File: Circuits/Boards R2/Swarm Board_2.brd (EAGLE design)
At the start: 54.9 x 63.6 mm, 94 parts, among them CON1 ISP(2X3), CON2 MAIN_CONNECTOR, CON3 FTDI_3PIN, CON4 POWERJUMPER, T1 NPN2N2222, T10 TEFT4300, T11 NPN2N2222, T13 NPN2N2222, T14 NPN2N2222, T15 NPN2N2222, T16 NPN2N2222, T17 NPN2N2222, T18 NPN2N2222, T2 NPN2N2222, T3 NPN2N2222, T4 TEFT4300, T5 TEFT4300, T6 TEFT4300, T7 TEFT4300, T8 TEFT4300, T9 TEFT4300, U1 ATMEGA324P, U2 MCP73833

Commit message: updated R2 board
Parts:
- CON4: value POWERJUMPER -> HEADER_3X1; device Mechanical:PINHEADER(1X2) -> Mechanical:3PINHEADER_.100"
- moved CON4 1.27 mm to (21.6, 37.8)
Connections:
- net +VBAT: now also CON4.2; no longer CON4.1
- net N$29: now also CON4.1; no longer CON4.2
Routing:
- net N$29: track 11.7 -> 17.9 mm
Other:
- board text added: "+3V"
- board text added: "B+"
- board text added: "B-"
- board text added: "MA+"
- board text added: "MA-"
- board text added: "MB+"
- board text added: "MB-"
- board text added: "PA1"
- board text added: "PA2"
- board text added: "PA3"
- board text added: "PA4T"
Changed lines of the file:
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@@
 <?xml version="1.0" encoding="utf-8"?>
 <!DOCTYPE eagle SYSTEM "eagle.dtd">
-<eagle version="6.2">
+<eagle version="6.3">
 <drawing>
 <settings>
@@
 <wire x1="4.318" y1="47.625" x2="59.182" y2="47.625" width="0.2032" layer="20" curve="-120"/>
 <wire x1="4.318" y1="15.748" x2="59.182" y2="15.748" width="0.2032" layer="20" curve="120"/>
+<text x="27.051" y="48.387" size="0.8128" layer="22" rot="MR270">B+</text>
+<text x="27.178" y="42.164" size="0.8128" layer="22" rot="MR270">B-</text>
+<text x="30.353" y="46.863" size="0.8128" layer="22" rot="MR90">GND</text>
+<text x="28.321" y="46.863" size="0.8128" layer="22" rot="MR90">+3V</text>
+<text x="37.338" y="42.164" size="0.8128" layer="22" rot="MR270">MB-</text>
+<text x="35.179" y="42.164" size="0.8128" layer="22" rot="MR270">MB+</text>
+<text x="37.211" y="49.149" size="0.8128" layer="22" rot="MR270">MA-</text>
+<text x="35.179" y="49.149" size="0.8128" layer="22" rot="MR270">MA+</text>
+<text x="33.02" y="49.911" size="0.8128" layer="22" rot="MR270">PA4T</text>
+<text x="29.21" y="42.164" size="0.8128" layer="22" rot="MR270">PA3</text>
+<text x="31.242" y="42.164" size="0.8128" layer="22" rot="MR270">PA2</text>
+<text x="33.274" y="42.164" size="0.8128" layer="22" rot="MR270">PA1</text>
 </plain>
 <attributes>
@@
 </class>
 </classes>
-<designrules>
+<designrules name="default">
 <description language="en">&lt;b&gt;EAGLE Design Rules&lt;/b&gt;
 &lt;p&gt;
@@
 </element>
 <element name="B1" library="Passive" package="PIEZOBUZZER" value="PIEZOBUZZERPTH" x="41.402" y="10.033"/>
-<element name="CON4" library="Mechanical" package="PINHEADER(1X2)" value="POWERJUMPER" x="21.59" y="39.116" rot="R90"/>
+<element name="CON4" library="Mechanical" package="3PINHEADER_.100&quot;" value="HEADER_3X1" x="21.59" y="37.846" rot="R90"/>
 </elements>
 <signals>
@@
 <wire x1="10.541" y1="17.950146875" x2="10.16" y2="18.542" width="0.254" layer="1"/>
 <wire x1="10.541" y1="17.950146875" x2="5.7785" y2="15.6845" width="0.4064" layer="16"/>
-<wire x1="11.944" y1="44.435478125" x2="13.6906" y2="43.64485" width="0.254" layer="1"/>
-<wire x1="11.944" y1="44.435478125" x2="9.271" y2="43.350146875" width="0.254" layer="1"/>
+<wire x1="11.944" y1="44.435478125" x2="13.6906" y2="43.64485" width="0.4064" layer="1"/>
+<wire x1="11.944" y1="44.435478125" x2="9.271" y2="43.350146875" width="0.4064" layer="1"/>
 <wire x1="5.461" y1="39.624" x2="9.187146875" y2="43.350146875" width="0.4064" layer="16"/>
 <wire x1="9.187146875" y1="43.350146875" x2="9.271" y2="43.350146875" width="0.3048" layer="16"/>
@@
 <wire x1="38.608" y1="24.765" x2="38.608" y2="25.997" width="0.3048" layer="1"/>
 <wire x1="38.608" y1="30.734" x2="38.608" y2="25.997" width="0.3048" layer="1"/>
-<wire x1="35.814" y1="32.547" x2="35.814" y2="30.734" width="0.3048" layer="1"/>
 <wire x1="27.559" y1="27.547" x2="27.297" y2="27.678" width="0.254" layer="1"/>
 <wire x1="27.297" y1="27.678" x2="25.908" y2="26.289" width="0.3048" layer="1"/>
@@
 <wire x1="45.593" y1="35.814" x2="46.482" y2="35.814" width="0.3048" layer="1"/>
 <wire x1="46.482" y1="35.814" x2="49.784" y2="39.116" width="0.3048" layer="1"/>
-<wire x1="35.814" y1="30.734" x2="38.608" y2="30.734" width="0.3048" layer="1"/>
 <wire x1="46.431" y1="43.266" x2="48.047" y2="43.266" width="0.3048" layer="1"/>
 <wire x1="48.047" y1="43.266" x2="48.895" y2="42.418" width="0.3048" layer="1"/>
@@
 <wire x1="49.784" y1="40.894" x2="48.907" y2="41.771" width="0.3048" layer="1"/>
 <wire x1="48.907" y1="41.771" x2="48.895" y2="41.771" width="0.3048" layer="1"/>
+<wire x1="35.814" y1="32.547" x2="35.814" y2="31.369" width="0.254" layer="1"/>
+<wire x1="35.814" y1="31.369" x2="36.449" y2="30.734" width="0.254" layer="1"/>
+<wire x1="36.449" y1="30.734" x2="38.608" y2="30.734" width="0.254" layer="1"/>
 </signal>
 <signal name="GND">
@@
 <wire x1="14.605" y1="30.341" x2="14.605" y2="31" width="0.254" layer="1"/>
 <wire x1="14.605" y1="31" x2="13.728" y2="31.877" width="0.254" layer="1"/>
-<contactref element="CON4" pad="1"/>
-<wire x1="21.59" y1="37.846" x2="20.955" y2="37.846" width="0.4064" layer="16"/>
 <wire x1="20.955" y1="37.846" x2="17.907" y2="40.894" width="0.4064" layer="16"/>
 <wire x1="17.907" y1="40.894" x2="16.637" y2="40.894" width="0.4064" layer="16"/>
+<contactref element="CON4" pad="2"/>
+<wire x1="20.955" y1="37.846" x2="21.59" y2="37.846" width="0.4064" layer="16"/>
 </signal>
 <signal name="+VCHG">
@@
 <signal name="N$29">
 <contactref element="CON2" pad="7"/>
-<contactref element="CON4" pad="2"/>
 <wire x1="26.75" y1="45.45" x2="20.939" y2="45.45" width="0.4064" layer="1"/>
 <wire x1="20.939" y1="45.45" x2="20.32" y2="44.831" width="0.4064" layer="1"/>
 <wire x1="20.32" y1="44.831" x2="20.32" y2="43.688" width="0.4064" layer="1"/>
-<wire x1="20.32" y1="43.688" x2="21.59" y2="42.418" width="0.4064" layer="1"/>
-<wire x1="21.59" y1="42.418" x2="21.59" y2="40.386" width="0.4064" layer="1"/>
+<contactref element="CON4" pad="1"/>
+<wire x1="20.32" y1="43.688" x2="22.987" y2="41.021" width="0.4064" layer="1"/>
+<wire x1="22.987" y1="41.021" x2="22.987" y2="36.703" width="0.4064" layer="1"/>
+<wire x1="22.987" y1="36.703" x2="21.59" y2="35.306" width="0.4064" layer="1"/>
 </signal>
 </signals>

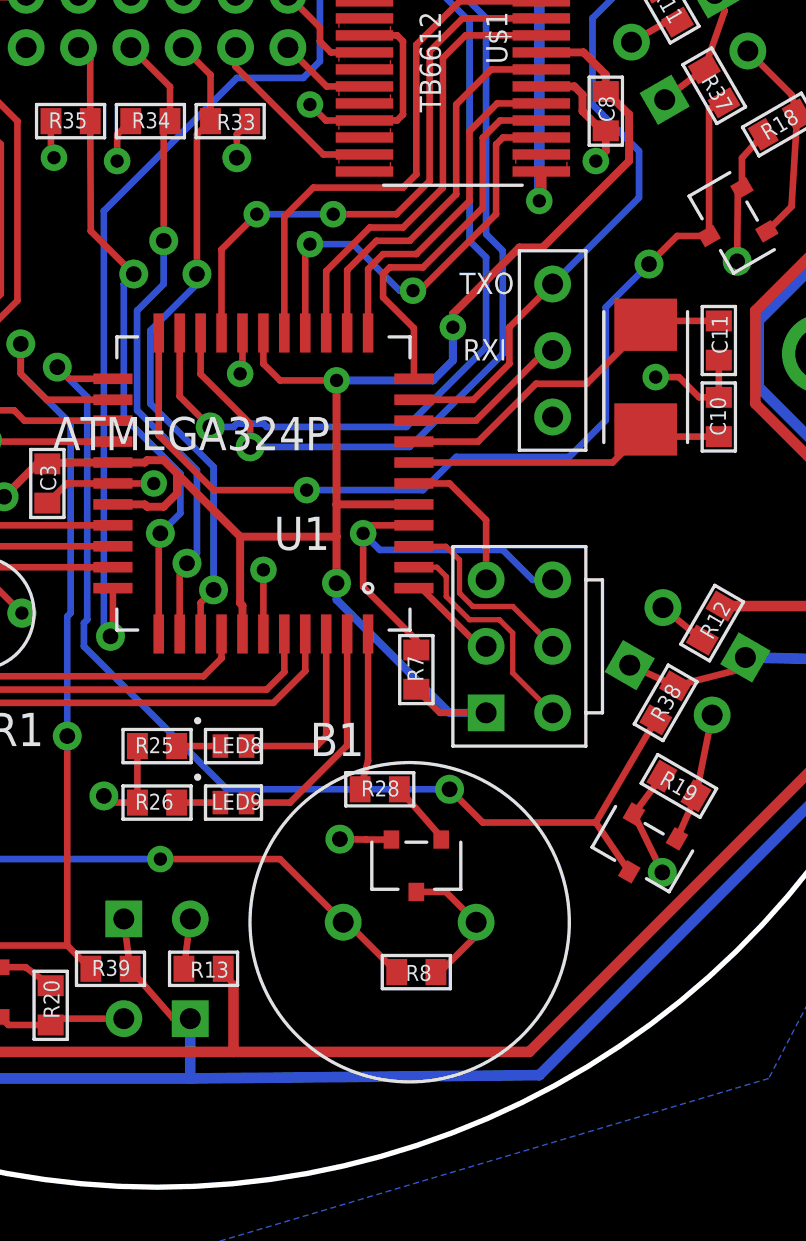
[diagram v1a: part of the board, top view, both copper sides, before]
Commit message: changed spacing on ISP header
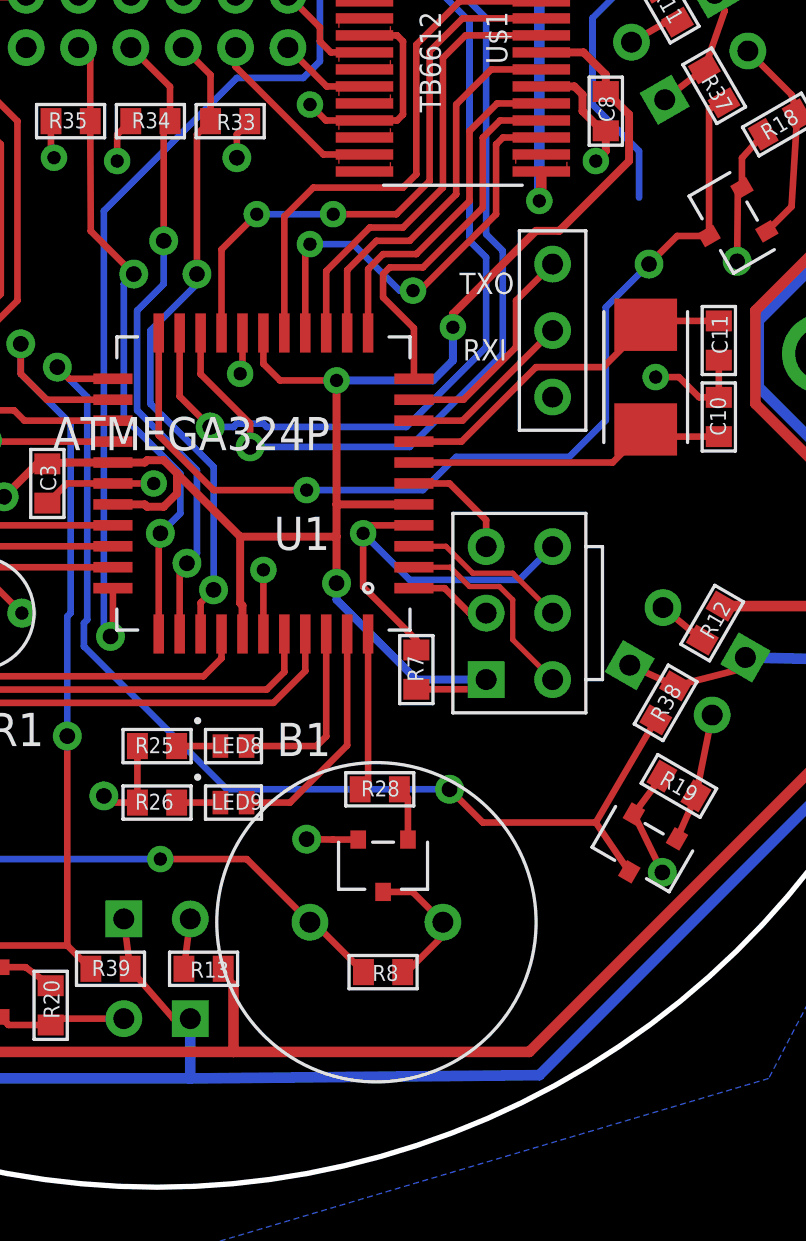
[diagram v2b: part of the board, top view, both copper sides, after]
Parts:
- moved B1 1.27 mm to (40.1, 10.0)
- moved CON1 1.27 mm to (45.6, 21.8)
- moved R8 1.27 mm to (40.4, 8.13)
- moved T1 1.27 mm to (40.4, 12.2)
- moved CON3 0.76 mm to (46.9, 32.6)
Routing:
- net DATAANTENNA: track 32.2 -> 28.1 mm
- net +3V: track 378.4 -> 376.4 mm
- net N$5: track 7.63 -> 6.36 mm
- net GND: track 116.0 -> 114.7 mm
- net N$3: track 8.94 -> 7.97 mm
- net N$26: track 2.76 -> 2.06 mm
- net N$6: track 15.3 -> 15.9 mm

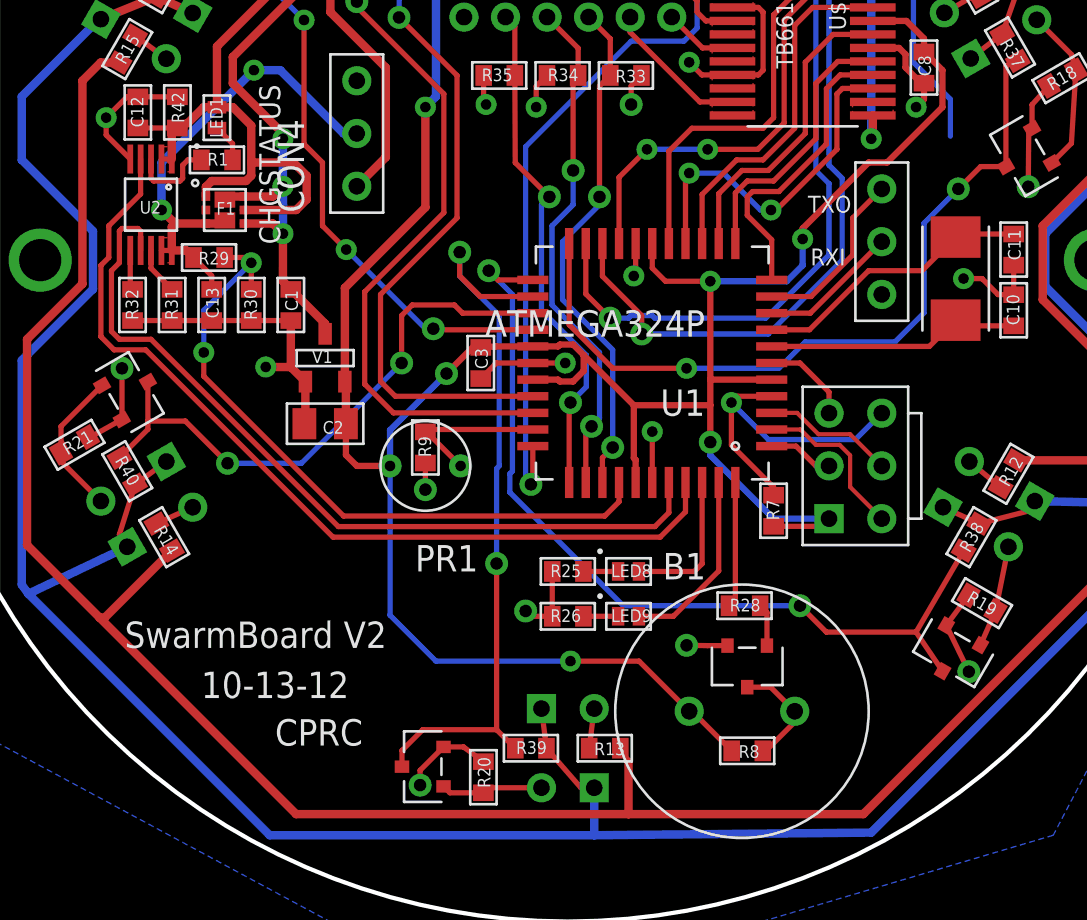
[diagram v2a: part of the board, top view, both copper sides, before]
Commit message: 
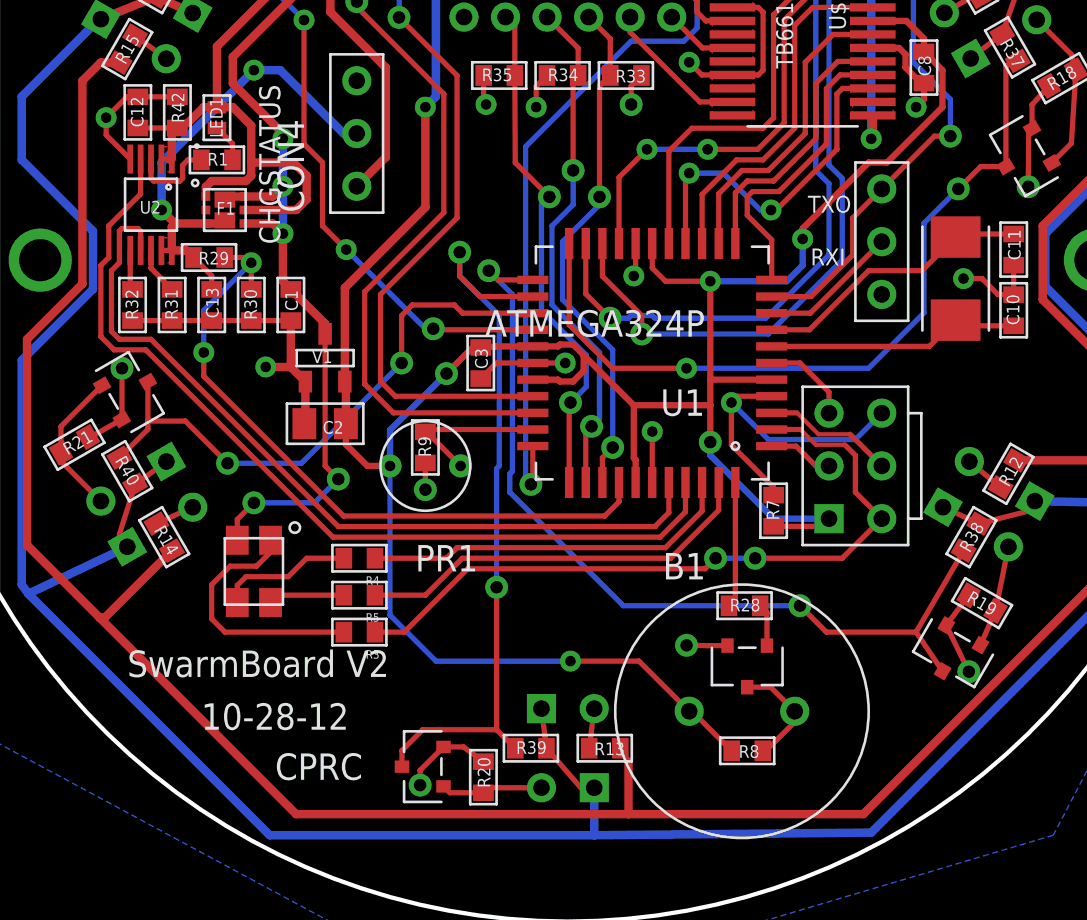
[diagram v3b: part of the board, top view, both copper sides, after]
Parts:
- removed LED8: red, Passive:LED0603
- removed LED9: green, Passive:LED0603
- removed R25, R26: 750, Passive:0603
- added LED10: SMD_RGB, Passive:PLCC4
- added R3: 180, Passive:0603
- added R4, R5: 70, Passive:0603
- R10, R11, R12, R13, R14, R15: value (none) -> 100
- R17, R18, R19, R20, R21, R24, R27: value (none) -> 10k
- R22: value (none) -> 15
- R36, R37, R38, R39, R40, R41: value (none) -> 4.7k
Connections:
- net N$2 renamed MOSI
- net N$5 renamed SCK
- net N$6 renamed RESET
- removed net N$20: LED8.1, R25.2
- removed net N$21: LED9.1, R26.2
- removed net N$3: CON1.6, U1.2
- new net MISO: CON1.6, R3.1, U1.2
- new net N$30: LED10.1, R3.2
- new net N$31: LED10.3, R4.2
- new net N$32: LED10.4, R5.2
- net +VRAW: now also LED10.2
- net GND: no longer R25.1, R26.1
- net LED1: now also R4.1; no longer LED8.2
- net LED2: now also R5.1; no longer LED9.2
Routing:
- net MISO: track 0.00 -> 34.8 mm, vias 0 -> 2
- net +VRAW: track 71.3 -> 85.2 mm, vias 5 -> 7
- net N$30: track 0.00 -> 12.3 mm
- net LED1: track 7.11 -> 18.1 mm
- net LED2: track 9.01 -> 19.6 mm
- net N$3: track 7.97 -> 0.00 mm
- net N$31: track 0.00 -> 6.50 mm
- net DATAANTENNA: track 28.1 -> 32.4 mm, vias 1 -> 2
- net N$32: track 0.00 -> 3.68 mm
- net GND: track 114.7 -> 111.1 mm, vias 23 -> 22
- net N$21: track 1.67 -> 0.00 mm
- net N$20: track 1.67 -> 0.00 mm
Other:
- board text added: "10-28-12"
- board text removed: "10-13-12"

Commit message: 
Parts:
- R33, R34, R35: value (none) -> 20k
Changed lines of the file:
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@@
 <attribute name="VALUE" x="29.464" y="56.569" size="0.4064" layer="27" rot="R270"/>
 </element>
-<element name="R33" library="Passive" package="0603" value="" x="34.544" y="40.64" smashed="yes" rot="R180">
+<element name="R33" library="Passive" package="0603" value="20k" x="34.544" y="40.64" smashed="yes" rot="R180">
 <attribute name="NAME" x="35.514" y="40.913" size="0.6096" layer="25" rot="R180"/>
 <attribute name="VALUE" x="35.614" y="41.91" size="0.4064" layer="27" rot="R180"/>
 </element>
-<element name="R34" library="Passive" package="0603" value="" x="31.496" y="40.64" smashed="yes">
+<element name="R34" library="Passive" package="0603" value="20k" x="31.496" y="40.64" smashed="yes">
 <attribute name="NAME" x="30.78" y="40.367" size="0.6096" layer="25"/>
 <attribute name="VALUE" x="30.426" y="39.37" size="0.4064" layer="27"/>
 </element>
-<element name="R35" library="Passive" package="0603" value="" x="28.448" y="40.64" smashed="yes">
+<element name="R35" library="Passive" package="0603" value="20k" x="28.448" y="40.64" smashed="yes">
 <attribute name="NAME" x="27.605" y="40.367" size="0.6096" layer="25"/>
 <attribute name="VALUE" x="27.378" y="39.37" size="0.4064" layer="27"/>
